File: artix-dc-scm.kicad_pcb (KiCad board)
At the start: 8 copper layers, 90 x 120.4 mm, 347 parts, among them IC1 TPS54561, J1 WE-RJ45_7499111121A, J10 61300611121, J11 DC_SOCKET, J12 S2B-PH-K-S_LF__SN_, J13 62000311121, J2 1-2199230-6, J3 543630489, J4 M20-7830642, J5 SFF-TA-1002-4C+, J6 0878311420, J7 61301021121, J8 61301021121, J9 61301221121, Q1 IRLML6402TRPBF, Q10 2N7002, Q11 2N7002, Q2 IRLML6402TRPBF, Q3 IRLML6402TRPBF, Q4 IRLML6402TRPBF, Q5 IRLML6402TRPBF, Q6 IRLML6402TRPBF, Q7 2N7002, Q8 2N7002, Q9 2N7002, U1 KSZ9031RNXCA, U10 TPS62823DLCT, U11 TPS62823DLCT, U12 TPS62823DLCT, U13 TPS62823DLCT, U14 XC7A100T-FGG484, U15 SN74LVC1G08DCKR, U16 SN74LS08DBR, U2 W25Q32JVSSIQ_TR, U3 W25Q32JVSSIQ_TR, U4 W25Q32JVSSIQ_TR, U5 W25Q32JVSSIQ_TR, U6 NVT2008DQ,115, U7 AS4C256M16D3, U8 TPS51200DRC, U9 LM3881MME_NOPB, Y1 ABM8G-25.000MHZ-18-D2Y-T

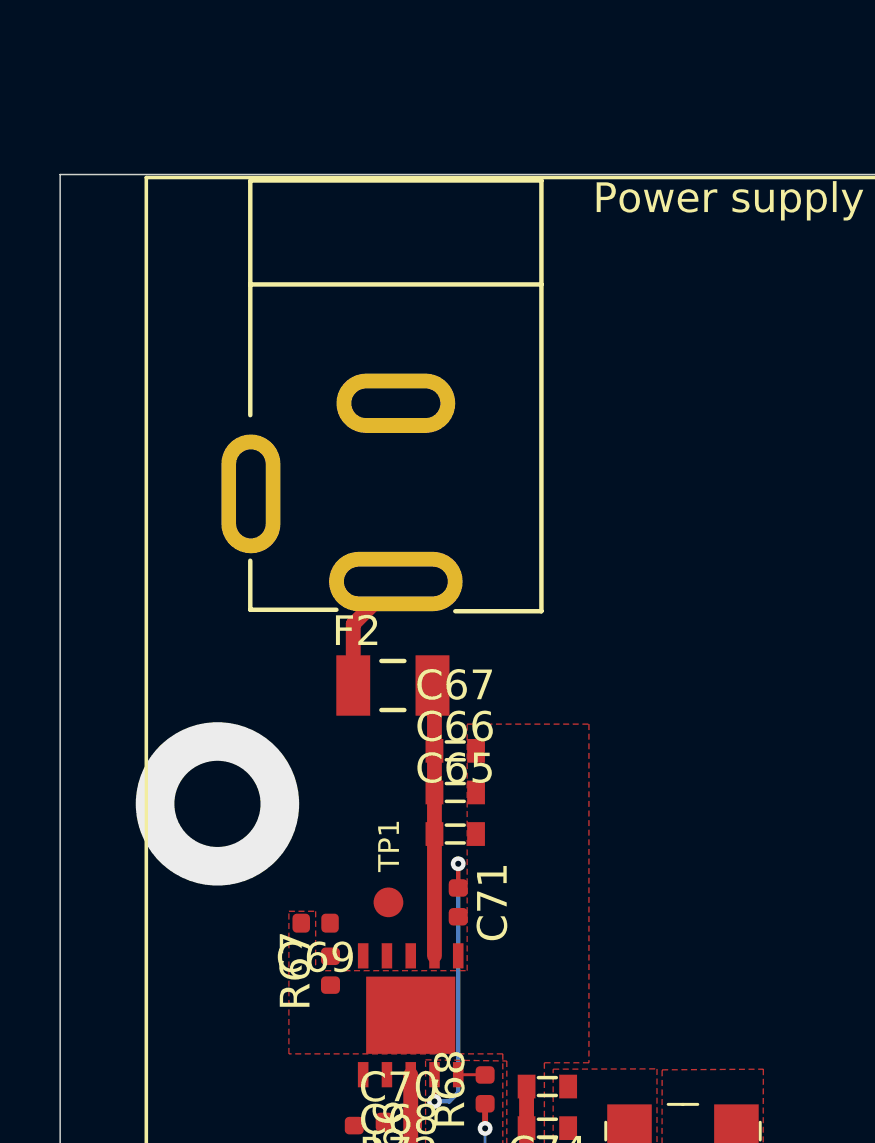
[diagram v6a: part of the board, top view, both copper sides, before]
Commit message: Removed DC connector
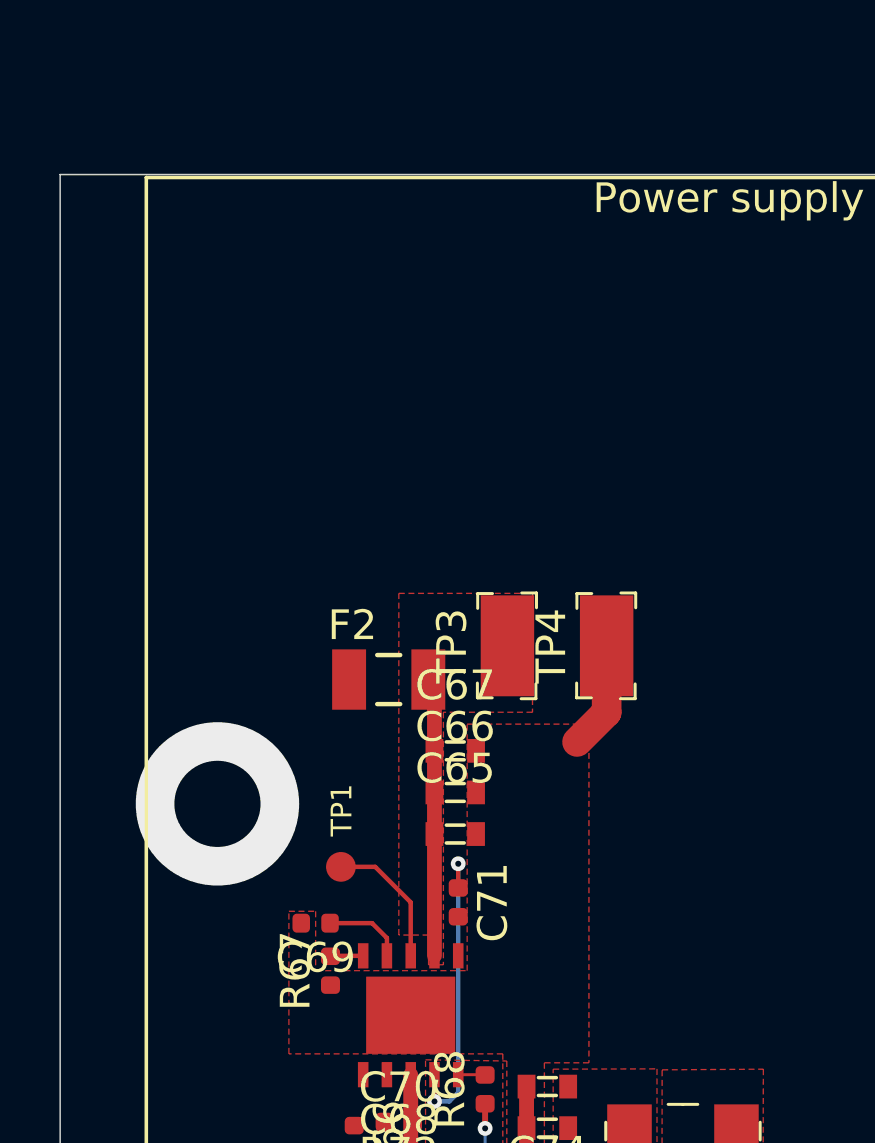
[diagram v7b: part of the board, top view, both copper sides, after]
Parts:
- removed J11: DC_SOCKET, artix-dc-scm-footprints:DC_SOCKET
- added TP3: RCW-0C, artix-dc-scm-footprints:PROBE_PAD_1206, F.Cu at (75.2, 74.8)
- added TP4: RCW-0C, artix-dc-scm-footprints:PROBE_PAD_1206, F.Cu at (78.5, 74.8)
- moved TP1 2.00 mm to (69.5, 82.2)
- moved F2 0.24 mm to (71.2, 75.9)
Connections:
- F1 pad 1: PCIe_12V -> P12V_AUX
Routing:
- net Net-(IC1-Pad3): track 0.00 -> 4.64 mm
- net Net-(F2-Pad1): track 4.09 -> 0.00 mm
- net GND: track 19.7 -> 23.3 mm
- net Net-(C69-Pad1): track 0.00 -> 2.72 mm
- net Net-(IC1-Pad5): track 0.00 -> 1.11 mm
- added copper zone on F.Cu, net VCC12V

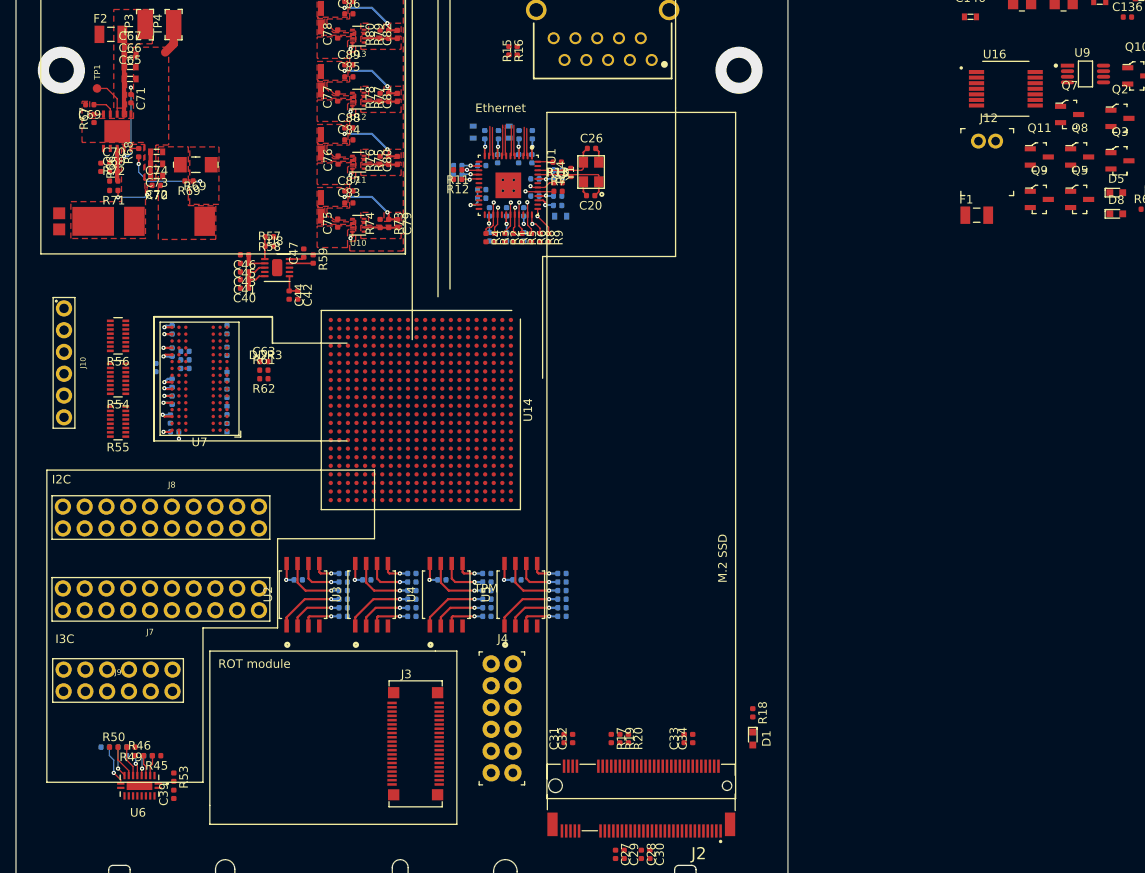
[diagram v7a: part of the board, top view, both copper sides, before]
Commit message: Removed debug headers
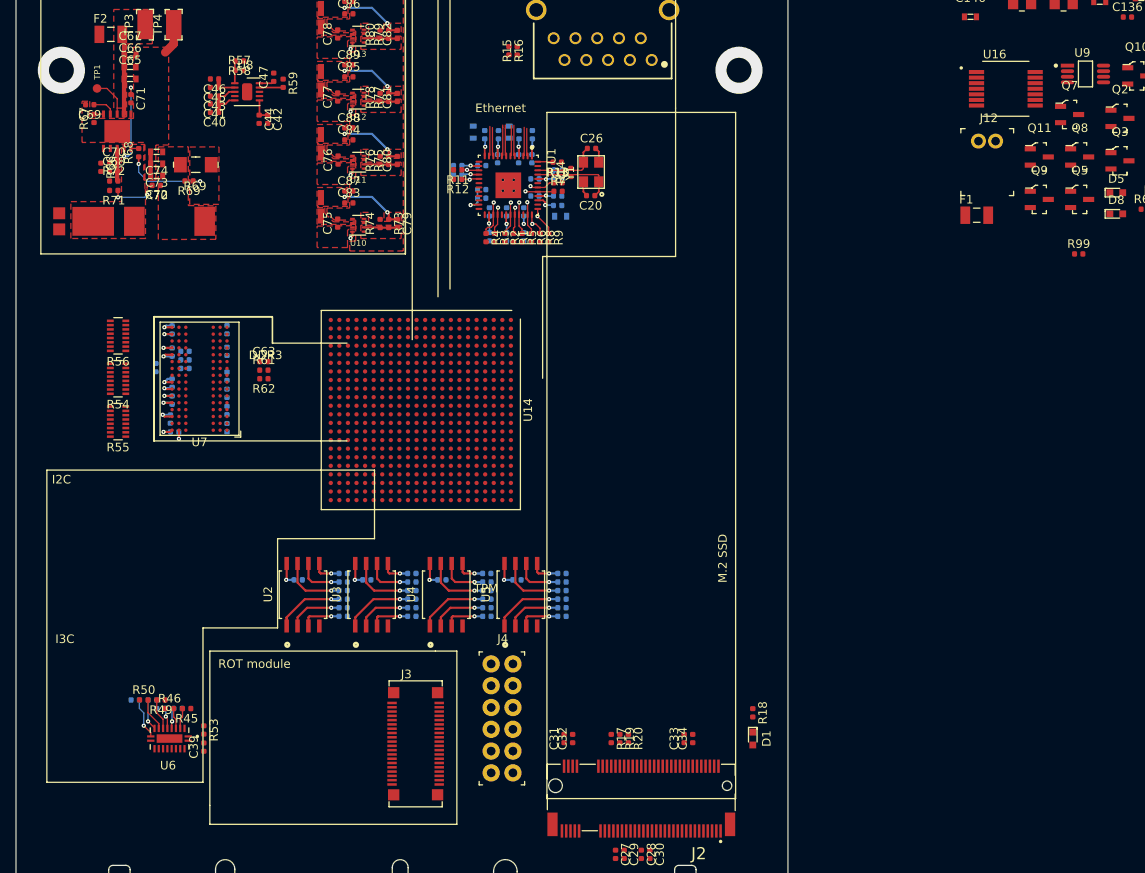
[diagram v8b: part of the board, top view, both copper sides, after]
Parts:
- removed J10: 61300611121, artix-dc-scm-footprints:61300611121
- removed J7, J8: 61301021121, artix-dc-scm-footprints:61301021121
- removed J9: 61301221121, artix-dc-scm-footprints:61301221121
- added R99: R_1k_0402, artix-dc-scm-footprints:0402-res, F.Cu at (184.0, 101.5)
- moved C40 20.8 mm to (83.2, 85.0)
- moved C41 20.8 mm to (83.2, 84.0)
- moved C42 20.8 mm to (89.5, 85.8)
- moved C43 20.8 mm to (83.2, 83.1)
- moved C44 20.8 mm to (88.5, 85.8)
- moved C45 20.8 mm to (83.2, 82.1)
- moved C46 20.8 mm to (83.2, 81.1)
- moved C47 20.8 mm to (90.2, 80.9)
- moved R57 20.8 mm to (86.2, 80.1)
- moved R58 20.8 mm to (86.2, 79.0)
- moved R59 20.8 mm to (91.2, 81.6)
- moved U8 20.8 mm to (86.8, 82.8)
- moved C39 6.52 mm to (82.0, 159.0)
- moved R45 6.52 mm to (80.0, 154.5)
- moved R46 6.52 mm to (78.0, 154.5)
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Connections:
- Q1 pad 1: /Power supply/VCCIO_EN_N -> /Power supply/VCCIO_EN
- Q2 pad 1: /Power supply/VCCIO_EN_N -> /Power supply/VCCIO_EN
- Q3 pad 1: /Power supply/VCCAUX_EN_N -> /Power supply/VCCAUX_EN
- Q4 pad 1: /Power supply/VCCAUX_EN_N -> /Power supply/VCCAUX_EN
- Q5 pad 1: /Power supply/VCCINT_EN_N -> /Power supply/VCCINT_EN
- Q6 pad 1: /Power supply/VCCIO_EN_N -> /Power supply/VCCIO_EN
- U14 pad A18: I3C0_SCL -> I3C[0]_SCL_3V3
- U14 pad A19: I3C1_SDA -> I3C[1]_SDA_3V3
- U14 pad A20: I3C0_SDA -> I3C[0]_SDA_3V3
- U14 pad C20: I3C3_SDA -> I3C[3]_SDA_3V3
- U14 pad C22: I3C3_SCL -> I3C[3]_SCL_3V3
- U14 pad D20: I3C2_SCL -> I3C[2]_SCL_3V3
- U14 pad F19: I3C1_SCL -> I3C[1]_SCL_3V3
- U14 pad F20: I3C2_SDA -> I3C[2]_SDA_3V3
- U6 pad 10: I3C[3]_SCL_3V3 -> I3C[0]_SCL_3V3
- U6 pad 11: I3C[3]_SCL_1V0 -> I3C[0]_SCL
- U6 pad 12: I3C[3]_SDA_1V0 -> I3C[0]_SDA
- U6 pad 13: I3C[2]_SCL_1V0 -> I3C[1]_SCL
- U6 pad 14: I3C[2]_SDA_1V0 -> I3C[1]_SDA
- U6 pad 15: I3C[1]_SCL_1V0 -> I3C[2]_SCL
- U6 pad 16: I3C[1]_SDA_1V0 -> I3C[2]_SDA
- U6 pad 17: I3C[0]_SCL_1V0 -> I3C[3]_SCL
- U6 pad 18: I3C[0]_SDA_1V0 -> I3C[3]_SDA
- U6 pad 3: I3C[0]_SDA_3V3 -> I3C[3]_SDA_3V3
- U6 pad 4: I3C[0]_SCL_3V3 -> I3C[3]_SCL_3V3
- U6 pad 5: I3C[1]_SDA_3V3 -> I3C[2]_SDA_3V3
- U6 pad 6: I3C[1]_SCL_3V3 -> I3C[2]_SCL_3V3
- U6 pad 7: I3C[2]_SDA_3V3 -> I3C[1]_SDA_3V3
- U6 pad 8: I3C[2]_SCL_3V3 -> I3C[1]_SCL_3V3
- U6 pad 9: I3C[3]_SDA_3V3 -> I3C[0]_SDA_3V3
